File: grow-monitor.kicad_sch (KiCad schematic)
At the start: 68 parts, among them J1 PH 2.0, J2 I2C1, J3 DS18B20, M1 M5StampS3, M2 AHT21B, P1 PCB_Patch, Q1 AO3401A, Q2 ALS-PT19-315C, Q3 AO3401A, Q4 2N7002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

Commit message: More improvements
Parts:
- JP5, JP6, TP1, TP10, TP11, TP2, TP3, TP6, TP7, TP8, TP9: footprint TestPoint:TestPoint_Pad_1.0x1.0mm -> local:TestPoint_Pad_1.0x1.0mm
- renumbered TP5 to C7
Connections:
- net CALIB: now also RN1.2 (R2.1); no longer RN1.1 (R1.1)
- net at D1.2 (A): now also RN1.1 (R1.1); no longer RN1.2 (R2.1)
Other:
- moved on the sheet: D1, SW2
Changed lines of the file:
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@@
 	)
 	(junction
-		(at 135.89 38.1)
+		(at 161.29 166.37)
 		(diameter 0)
 		(color 0 0 0 0)
 	)
 	(junction
-		(at 31.75 54.61)
+		(at 135.89 38.1)
 		(diameter 0)
 		(color 0 0 0 0)
 	)
 	(junction
-		(at 184.15 53.34)
+		(at 31.75 54.61)
 		(diameter 0)
 		(color 0 0 0 0)
 	)
 	(junction
-		(at 166.37 166.37)
+		(at 184.15 53.34)
 		(diameter 0)
 		(color 0 0 0 0)
@@
 	(wire
 		(pts
-			(xy 161.29 162.56) (xy 161.29 165.1)
+			(xy 171.45 160.02) (xy 171.45 173.99)
 		)
 		(stroke
@@
 	(wire
 		(pts
-			(xy 166.37 160.02) (xy 166.37 166.37)
-		)
-		(stroke
-			(width 0)
-			(type default)
-		)
-	)
-	(wire
-		(pts
 			(xy 151.13 50.8) (xy 148.59 50.8)
 		)
@@
 	(wire
 		(pts
-			(xy 166.37 182.88) (xy 166.37 186.69)
+			(xy 161.29 182.88) (xy 161.29 186.69)
 		)
 		(stroke
@@
 	(wire
 		(pts
-			(xy 166.37 166.37) (xy 172.72 166.37)
+			(xy 161.29 166.37) (xy 167.64 166.37)
 		)
 		(stroke
@@
 	(wire
 		(pts
-			(xy 158.75 160.02) (xy 166.37 160.02)
-		)
-		(stroke
-			(width 0)
-			(type default)
-		)
-	)
-	(wire
-		(pts
 			(xy 151.13 184.15) (xy 151.13 186.69)
 		)
@@
 	(wire
 		(pts
-			(xy 166.37 166.37) (xy 166.37 172.72)
+			(xy 161.29 162.56) (xy 161.29 166.37)
 		)
 		(stroke
@@
 	(wire
 		(pts
-			(xy 161.29 172.72) (xy 161.29 186.69)
+			(xy 171.45 181.61) (xy 171.45 186.69)
 		)
 		(stroke
@@
 	(wire
 		(pts
+			(xy 161.29 166.37) (xy 161.29 172.72)
+		)
+		(stroke
+			(width 0)
+			(type default)
+		)
+	)
+	(wire
+		(pts
 			(xy 194.31 143.51) (xy 194.31 148.59)
 		)
@@
 	(wire
 		(pts
+			(xy 171.45 160.02) (xy 158.75 160.02)
+		)
+		(stroke
+			(width 0)
+			(type default)
+		)
+	)
+	(wire
+		(pts
 			(xy 93.98 55.88) (xy 93.98 58.42)
 		)
@@
 	)
 	(label "CALIB"
-		(at 172.72 166.37 180)
+		(at 167.64 166.37 180)
 		(fields_autoplaced yes)
 		(effects
@@
 			)
 		)
-		(property "Footprint" "TestPoint:TestPoint_Pad_1.0x1.0mm"
+		(property "Footprint" "local:TestPoint_Pad_1.0x1.0mm"
 			(at 109.22 107.95 0)
 			(effects
@@
 	(symbol
 		(lib_id "power:GND")
-		(at 161.29 186.69 0)
+		(at 171.45 186.69 0)
 		(unit 1)
 		(exclude_from_sim no)
@@
 		(fields_autoplaced yes)
 		(property "Reference" "#PWR026"
-			(at 161.29 193.04 0)
+			(at 171.45 193.04 0)
 			(effects
 				(font
@@
 		)
 		(property "Value" "GND"
-			(at 161.29 190.8231 0)
+			(at 171.45 190.8231 0)
 			(effects
 				(font
@@
 		)
 		(property "Footprint" ""
-			(at 161.29 186.69 0)
+			(at 171.45 186.69 0)
 			(effects
 				(font
@@
 		)
 		(property "Datasheet" ""
-			(at 161.29 186.69 0)
+			(at 171.45 186.69 0)
 			(effects
 				(font
@@
 		)
 		(property "Description" "Power symbol creates a global label with name \"GND\" , ground"
-			(at 161.29 186.69 0)
+			(at 171.45 186.69 0)
 			(effects
 				(font
@@
 			)
 		)
-		(property "Footprint" "TestPoint:TestPoint_Pad_1.0x1.0mm"
+		(property "Footprint" "local:TestPoint_Pad_1.0x1.0mm"
 			(at 19.05 125.73 0)
 			(effects
@@
 			)
 		)
-		(property "Footprint" "TestPoint:TestPoint_Pad_1.0x1.0mm"
+		(property "Footprint" "local:TestPoint_Pad_1.0x1.0mm"
 			(at 19.05 128.27 0)
 			(effects
@@
 			)
 		)
-		(property "Footprint" "TestPoint:TestPoint_Pad_1.0x1.0mm"
+		(property "Footprint" "local:TestPoint_Pad_1.0x1.0mm"
 			(at 107.95 102.87 0)
 			(effects
@@
 		(exclude_from_sim no)
 		(in_bom yes)
-		(on_board yes)
+		(on_board no)
 		(dnp no)
 		(fields_autoplaced yes)
@@
 			)
 		)
-		(property "Footprint" "TestPoint:TestPoint_Pad_1.0x1.0mm"
+		(property "Footprint" "local:TestPoint_Pad_1.0x1.0mm"
 			(at 234.95 175.26 0)
 			(effects
@@
 	(symbol
 		(lib_id "Switch:SW_Push")
-		(at 166.37 177.8 270)
+		(at 161.29 177.8 270)
 		(mirror x)
 		(unit 1)
@@
 		(dnp no)
 		(property "Reference" "SW2"
-			(at 170.942 181.61 90)
+			(at 165.862 181.61 90)
 			(effects
 				(font
@@
 		)
 		(property "Value" "CALIB"
-			(at 165.227 179.0121 90)
+			(at 160.147 179.0121 90)
 			(effects
 				(font
@@
 		)
 		(property "Footprint" "local:SW_Push_SPST_NO_432"
-			(at 171.45 177.8 0)
+			(at 166.37 177.8 0)
 			(effects
 				(font
@@
 		)
 		(property "Datasheet" "~"
-			(at 171.45 177.8 0)
+			(at 166.37 177.8 0)
 			(effects
 				(font
@@
 		)
 		(property "Description" "Push button switch, generic, two pins"
-			(at 166.37 177.8 0)
+			(at 161.29 177.8 0)
 			(effects
 				(font
@@
 		)
 		(property "LCSC" "C707339"
-			(at 166.37 177.8 0)
+			(at 161.29 177.8 0)
 			(effects
 				(font
@@
 	(symbol
 		(lib_id "Device:LED")
-		(at 161.29 168.91 90)
+		(at 171.45 177.8 90)
 		(unit 1)
 		(exclude_from_sim no)
@@
 		(dnp no)
 		(property "Reference" "D1"
-			(at 161.798 174.752 90)
+			(at 171.958 183.642 90)
 			(effects
 				(font
@@
 		)
 		(property "Value" "GREEN"
-			(at 157.988 166.116 90)
+			(at 168.148 175.006 90)
 			(effects
 				(font
@@
 		)
 		(property "Footprint" "LED_SMD:LED_0603_1608Metric"
-			(at 161.29 168.91 0)
+			(at 171.45 177.8 0)
 			(effects
 				(font
@@
 		)
 		(property "Datasheet" "~"
-			(at 161.29 168.91 0)
+			(at 171.45 177.8 0)
 			(effects
 				(font
@@
 		)
 		(property "Description" "Light emitting diode"
-			(at 161.29 168.91 0)
+			(at 171.45 177.8 0)
 			(effects
 				(font
@@
 		)
 		(property "LCSC" ""
-			(at 161.29 168.91 0)
+			(at 171.45 177.8 0)
 			(effects
 				(font
@@
 			)
 		)
-		(property "Footprint" "TestPoint:TestPoint_Pad_1.0x1.0mm"
+		(property "Footprint" "local:TestPoint_Pad_1.0x1.0mm"
 			(at 19.05 113.03 0)
 			(effects
@@
 		(on_board yes)
 		(dnp no)
-		(fields_autoplaced yes)
 		(property "Reference" "#PWR019"
 			(at 119.38 29.21 0)
@@
 		)
 		(property "Value" "+BATT_SW"
-			(at 119.38 21.2669 0)
+			(at 115.57 21.336 0)
 			(effects
 				(font
@@
 			)
 		)
-		(property "Footprint" "TestPoint:TestPoint_Pad_1.0x1.0mm"
+		(property "Footprint" "local:TestPoint_Pad_1.0x1.0mm"
 			(at 109.22 95.25 0)
 			(effects
@@
 			)
 		)
-		(property "Footprint" "TestPoint:TestPoint_Pad_1.0x1.0mm"
+		(property "Footprint" "local:TestPoint_Pad_1.0x1.0mm"
 			(at 109.22 113.03 0)
 			(effects
@@
 			)
 		)
-		(property "Footprint" "TestPoint:TestPoint_Pad_1.0x1.0mm"
+		(property "Footprint" "local:TestPoint_Pad_1.0x1.0mm"
 			(at 109.22 105.41 0)
 			(effects
@@
 			)
 		)
-		(property "Footprint" "TestPoint:TestPoint_Pad_1.0x1.0mm"
+		(property "Footprint" "local:TestPoint_Pad_1.0x1.0mm"
 			(at 107.95 97.79 0)
 			(effects
@@
 	(symbol
 		(lib_id "power:GND")
-		(at 166.37 186.69 0)
+		(at 161.29 186.69 0)
 		(unit 1)
 		(exclude_from_sim no)
@@
 		(fields_autoplaced yes)
 		(property "Reference" "#PWR029"
-			(at 166.37 193.04 0)
+			(at 161.29 193.04 0)
 			(effects
 				(font
@@
 		)
 		(property "Value" "GND"
-			(at 166.37 190.8231 0)
+			(at 161.29 190.8231 0)
 			(effects
 				(font
@@
 		)
 		(property "Footprint" ""
-			(at 166.37 186.69 0)
+			(at 161.29 186.69 0)
 			(effects
 				(font
@@
 		)
 		(property "Datasheet" ""
-			(at 166.37 186.69 0)
+			(at 161.29 186.69 0)
 			(effects
 				(font
@@
 		)
 		(property "Description" "Power symbol creates a global label with name \"GND\" , ground"
-			(at 166.37 186.69 0)
+			(at 161.29 186.69 0)
 			(effects
 				(font
@@
 		(on_board yes)
 		(dnp no)
-		(fields_autoplaced yes)
 		(property "Reference" "#FLG03"
 			(at 124.46 23.495 0)
@@
 		)
 		(property "Value" "PWR_FLAG"
-			(at 124.46 21.2669 0)
+			(at 127.762 21.336 0)
 			(effects
 				(font
@@
 		(on_board yes)
 		(dnp no)
-		(property "Reference" "TP5"
+		(property "Reference" "C7"
 			(at 93.218 179.832 90)
 			(effects
@@
 			(project "grow-monitor"
 				(path "/ff355f4c-e562-4fd3-bc17-978a5d849f6b"
-					(reference "TP5")
+					(reference "C7")
 					(unit 1)
 				)
@@
 			)
 		)
-		(property "Footprint" "TestPoint:TestPoint_Pad_1.0x1.0mm"
+		(property "Footprint" "local:TestPoint_Pad_1.0x1.0mm"
 			(at 109.22 100.33 0)
 			(effects

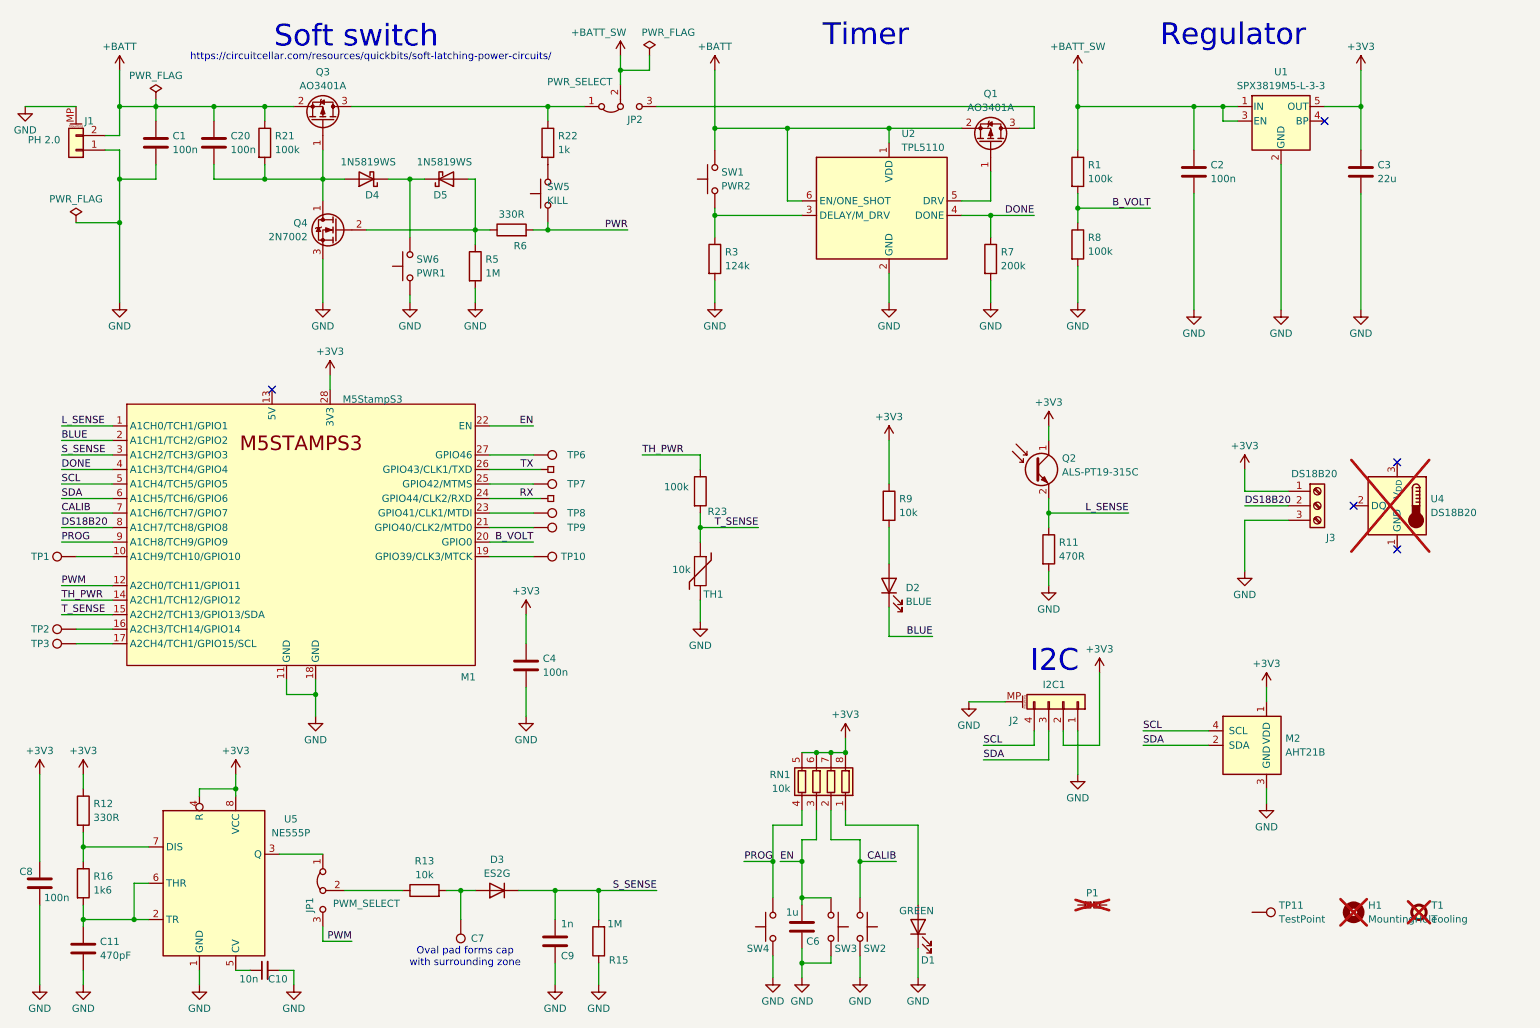
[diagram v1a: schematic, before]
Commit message: Switched jumpers to use stock cct by default
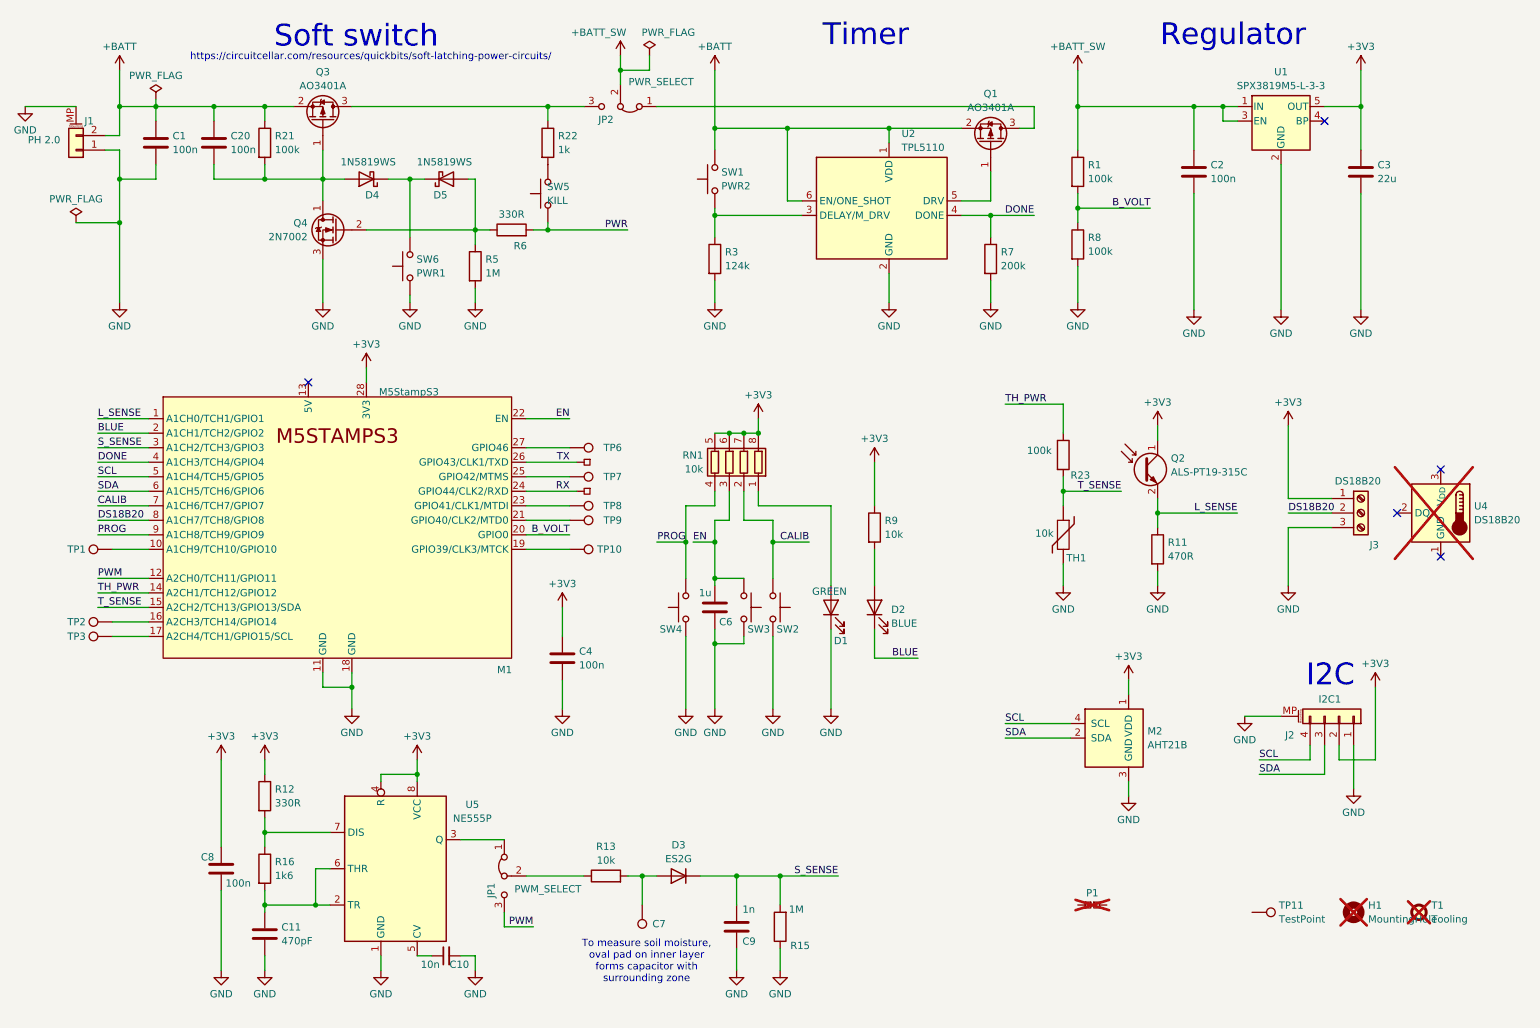
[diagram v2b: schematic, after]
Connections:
- net at Q3.3 (D), R22.1: now also JP2.3 (B); no longer JP2.1 (A)
- net at Q1.3 (D): now also JP2.1 (A); no longer JP2.3 (B)
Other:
- note added: "To measure soil moisture, oval pad on inner layer forms capacitor with surrounding zone"
- note removed: "Oval pad forms cap with surrounding zone"
- moved on the sheet: C10, C11, C4, C6, C7, C8, C9, D1, D2, D3, J2, J3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

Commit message: Added title, revision, email and date
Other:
- company: (none) -> mjd@afork.com
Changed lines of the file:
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@@
 	(generator_version "8.0")
 	(paper "A4")
+	(title_block
+		(date "5-Jan-2024")
+		(rev "1.0a")
+		(company "mjd@afork.com")
+	)
 	(junction
 		(at 138.43 91.44)

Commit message: Add caps
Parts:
- C3: value 22u -> 22u 25V; LCSC (none) -> C45783
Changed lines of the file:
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@@
 			)
 		)
-		(property "Value" "22u"
+		(property "Value" "22u 25V"
 			(at 251.841 46.9321 0)
 			(effects
@@
 			)
 		)
-		(property "LCSC" ""
+		(property "LCSC" "C45783"
 			(at 248.92 45.72 0)
 			(effects

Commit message: Convert to KiCad 9
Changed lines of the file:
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@@
 (kicad_sch
-	(version 20231120)
+	(version 20250114)
 	(generator "eeschema")
-	(generator_version "8.0")
+	(generator_version "9.0")
 	(paper "A4")
 	(title_block
@@
 		(company "mjd@afork.com")
 	)
+	(text "Regulator"
+		(exclude_from_sim no)
+		(at 226.568 21.844 0)
+		(effects
+			(font
+				(size 3.81 3.81)
+			)
+		)
+	)
+	(text "To measure soil moisture,\noval pad on inner layer\nforms capacitor with\nsurrounding zone"
+		(exclude_from_sim no)
+		(at 123.952 183.896 0)
+		(effects
+			(font
+				(size 1.27 1.27)
+			)
+		)
+	)
+	(text "I2C"
+		(exclude_from_sim no)
+		(at 243.586 133.858 0)
+		(effects
+			(font
+				(size 3.81 3.81)
+			)
+		)
+	)
+	(text "Timer"
+		(exclude_from_sim no)
+		(at 162.306 21.844 0)
+		(effects
+			(font
+				(size 3.81 3.81)
+			)
+		)
+	)
+	(text "https://circuitcellar.com/resources/quickbits/soft-latching-power-circuits/"
+		(exclude_from_sim no)
+		(at 75.692 25.654 0)
+		(effects
+			(font
+				(size 1.27 1.27)
+			)
+		)
+	)
+	(text "Soft switch"
+		(exclude_from_sim no)
+		(at 73.152 22.098 0)
+		(effects
+			(font
+				(size 3.81 3.81)
+			)
+		)
+	)
 	(junction
 		(at 138.43 91.44)
@@
 		)
 	)
-	(text "Regulator"
-		(exclude_from_sim no)
-		(at 226.568 21.844 0)
-		(effects
-			(font
-				(size 3.81 3.81)
-			)
-		)
-	)
-	(text "To measure soil moisture,\noval pad on inner layer\nforms capacitor with\nsurrounding zone"
-		(exclude_from_sim no)
-		(at 123.952 183.896 0)
-		(effects
-			(font
-				(size 1.27 1.27)
-			)
-		)
-	)
-	(text "I2C"
-		(exclude_from_sim no)
-		(at 243.586 133.858 0)
-		(effects
-			(font
-				(size 3.81 3.81)
-			)
-		)
-	)
-	(text "Timer"
-		(exclude_from_sim no)
-		(at 162.306 21.844 0)
-		(effects
-			(font
-				(size 3.81 3.81)
-			)
-		)
-	)
-	(text "https://circuitcellar.com/resources/quickbits/soft-latching-power-circuits/"
-		(exclude_from_sim no)
-		(at 75.692 25.654 0)
-		(effects
-			(font
-				(size 1.27 1.27)
-			)
-		)
-	)
-	(text "Soft switch"
-		(exclude_from_sim no)
-		(at 73.152 22.098 0)
-		(effects
-			(font
-				(size 3.81 3.81)
-			)
-		)
-	)
 	(label "SCL"
 		(at 27.94 99.06 0)
-		(fields_autoplaced yes)
 		(effects
 			(font
@@
 	(label "BLUE"
 		(at 171.45 130.81 180)
-		(fields_autoplaced yes)
 		(effects
 			(font
@@
 	(label "SCL"
 		(at 186.69 142.24 0)
-		(fields_autoplaced yes)
 		(effects
 			(font
@@
 	(label "RX"
 		(at 110.49 101.6 180)
-		(fields_autoplaced yes)
 		(effects
 			(font
@@
 	(label "B_VOLT"
 		(at 110.49 109.22 180)
-		(fields_autoplaced yes)
 		(effects
 			(font
@@
 	(label "S_SENSE"
 		(at 27.94 93.98 0)
-		(fields_autoplaced yes)
 		(effects
 			(font
@@
 	(label "DS18B20"
 		(at 27.94 106.68 0)
-		(fields_autoplaced yes)
 		(effects
 			(font
@@
 	(label "EN"
 		(at 132.08 110.49 0)
-		(fields_autoplaced yes)
 		(effects
 			(font
@@
 	(label "TH_PWR"
 		(at 27.94 119.38 0)
-		(fields_autoplaced yes)
 		(effects
 			(font
@@
 	(label "DS18B20"
 		(at 236.22 105.41 0)
-		(fields_autoplaced yes)
 		(effects
 			(font
@@
 	(label "T_SENSE"
 		(at 207.01 101.6 180)
-		(fields_autoplaced yes)
 		(effects
 			(font
@@
 	(label "PWM"
 		(at 104.14 177.8 180)
-		(fields_autoplaced yes)
 		(effects
 			(font
@@
 	(label "EN"
 		(at 110.49 88.9 180)
-		(fields_autoplaced yes)
 		(effects
 			(font
@@
 	(label "TH_PWR"
 		(at 186.69 86.36 0)
-		(fields_autoplaced yes)
 		(effects
 			(font
@@
 	(label "CALIB"
 		(at 152.4 110.49 180)
-		(fields_autoplaced yes)
 		(effects
 			(font
@@
 	(label "SDA"
 		(at 231.14 151.13 0)
-		(fields_autoplaced yes)
 		(effects
 			(font
@@
 	(label "SDA"
 		(at 186.69 144.78 0)
-		(fields_autoplaced yes)
 		(effects
 			(font
@@
 	(label "CALIB"
 		(at 27.94 104.14 0)
-		(fields_autoplaced yes)
 		(effects
 			(font
@@
 	(label "PWR"
 		(at 120.65 55.88 180)
-		(fields_autoplaced yes)
 		(effects
 			(font
@@
 	(label "BLUE"
 		(at 27.94 91.44 0)
-		(fields_autoplaced yes)
 		(effects
 			(font
@@
 	(label "L_SENSE"
 		(at 227.33 105.41 180)
-		(fields_autoplaced yes)
 		(effects
 			(font
@@
 	(label "DONE"
 		(at 27.94 96.52 0)
-		(fields_autoplaced yes)
 		(effects
 			(font
@@
 	(label "S_SENSE"
 		(at 157.48 168.91 180)
-		(fields_autoplaced yes)
 		(effects
 			(font
@@
 	(label "L_SENSE"
 		(at 27.94 88.9 0)
-		(fields_autoplaced yes)
 		(effects
 			(font
@@
 	(label "B_VOLT"
 		(at 212.09 52.07 180)
-		(fields_autoplaced yes)
 		(effects
 			(font
@@
 	(label "PWM"
 		(at 27.94 116.84 0)
-		(fields_autoplaced yes)
 		(effects
 			(font
@@
 	(label "PROG"
 		(at 27.94 109.22 0)
-		(fields_autoplaced yes)
 		(effects
 			(font
@@
 	(label "DONE"
 		(at 191.77 53.34 180)
-		(fields_autoplaced yes)
 		(effects
 			(font
@@
 	(label "PROG"
 		(at 130.81 110.49 180)
-		(fields_autoplaced yes)
 		(effects
 			(font
@@
 	(label "T_SENSE"
 		(at 27.94 121.92 0)
-		(fields_autoplaced yes)
 		(effects
 			(font
@@
 	(label "SDA"
 		(at 27.94 101.6 0)
-		(fields_autoplaced yes)
 		(effects
 			(font
@@
 	(label "SCL"
 		(at 231.14 148.59 0)
-		(fields_autoplaced yes)
 		(effects
 			(font
@@
 	(label "TX"
 		(at 110.49 96.52 180)
-		(fields_autoplaced yes)
 		(effects
 			(font
@@
 		)
 	)
+	(embedded_fonts no)
 )
